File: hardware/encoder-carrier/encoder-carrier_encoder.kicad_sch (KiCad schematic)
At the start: 3 parts, among them J1 PANEL, J2 STOP, SW1 EC11E15244G1

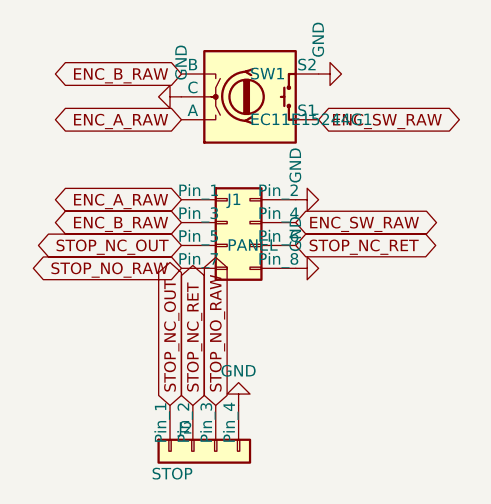
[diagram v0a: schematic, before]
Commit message: feat(hardware): JST XH connectors, re-placement and re-route, open fuse holder (T087, T021)
Connectors (T087, research R9/R10, contracts/connectors.md):
- J3 display JST XH 1x10 (same pin order as the IDC 2x5)
- J4 encoder JST XH 1x5 (A, GND, B, SW, GND), new J11 stop button
  JST XH 1x4 directly on the main board; an unplugged stop connector
  opens the NC loop like a pressed stop button
- encoder carrier: J1 JST XH 1x5, J2 (stop wires) removed
- schematic wire chains of the old connectors replaced by labels,
  connectivity checked pin by pin; ref netlists re-exported

Layout:
- XH connectors at the right edge, RESET/BOOT moved inside
- decoupling capacitors next to their IC pins (LDO 2.6/2.9 mm,
  MAX31856 2.3-3.7 mm, U7/U8/U9 2.2-4.3 mm, ESP32 5.1 mm)
- EMC: flyback diode D7 at the buzzer, 33 ohm SPI resistors at the
  module pins, C1 on the IRM-10-5 output path, thermal vias at the LDO
- re-routed with Freerouting 1.9.0 (2.5.0 compared and rejected),
  GND stitching and isolated GND groups connected
- manual rework by the user: USB D+/D- through the ESD array U4 at the
  connector, tightly coupled, CC2 connected, U4 pin 2 GND connected
- COV1 restored after an accidental delete, dangling stubs removed
- F1: Schurter OGN 0031.8201 open fuse holder instead of the FAB, whose
  carrier is pulled out axially and was blocked by RV1/IRM-10-5;
  L_FUSED re-routed

DRC with schematic parity: 0 errors, 0 unconnected (2 silk edge
warnings from the U1 footprint); check_schematic 0 errors for both
boards; ERC only the documented SDO exclusion.

Co-Authored-By: Claude Opus 5.5 <noreply@anthropic.com>
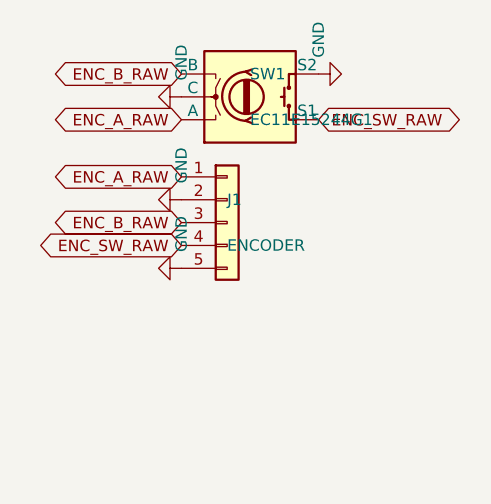
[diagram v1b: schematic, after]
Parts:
- removed J2: STOP, Connector_JST:JST_XH_B4B-XH-A_1x04_P2.50mm_Vertical, symbol Connector_Generic:Conn_01x04
- J1: value PANEL -> ENCODER; footprint Connector_IDC:IDC-Header_2x04_P2.54mm_Vertical -> Connector_JST:JST_XH_B5B-XH-A_1x05_P2.50mm_Vertical; symbol Connector_Generic:Conn_02x04_Odd_Even -> Connector_Generic:Conn_01x05; MPN Wannenstecker 2x4 RM2.54 -> JST B5B-XH-A
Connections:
- net STOP_NC_OUT is gone; now on net GND: J1.5 (Pin_5)
- net GND: no longer J1.8 (Pin_8)
- removed net STOP_NC_RET: J1.6 (Pin_6)
- removed net STOP_NO_RAW: J1.7 (Pin_7)
